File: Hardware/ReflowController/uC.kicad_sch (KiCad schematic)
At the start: 8 parts

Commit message: work on uC circuit. pin selection for the different IOs still pending
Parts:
- added NT10, NT11, NT12, NT13, NT14, NT15, NT16, NT17, NT18, NT19, NT2, NT20, NT3, NT8, NT9: NetTie_2, symbol Device:NetTie_2
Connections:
- new net FAN_1_EN: NT15.2
- new net FAN_2_EN: NT17.2
- new net HSS_1_EN: NT9.2
- new net HSS_2_EN: NT10.2
- new net HSS_3_EN: NT11.2
- new net HSS_4_EN: NT12.2
- new net PWM_BUZZER: NT2.2
- new net PWM_FAN_1: NT16.2
- new net PWM_FAN_2: NT18.2
- new net RELAY_1: NT13.2
- new net RELAY_2: NT14.2
- new net RESET_UI: NT8.2
- new net ~{INT_EMERGENCY_STOP}: NT19.2
- new net ~{INT_IO_EXPANDER}: NT3.2
- new net ~{TEMP_DATA_READY}: NT20.2
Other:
- note added: "FAN"
- note added: "IO"
- note added: "TEMP"
- note added: "UI"
- moved on the sheet: A1, NT1, NT4, NT5, NT6, NT7, R2

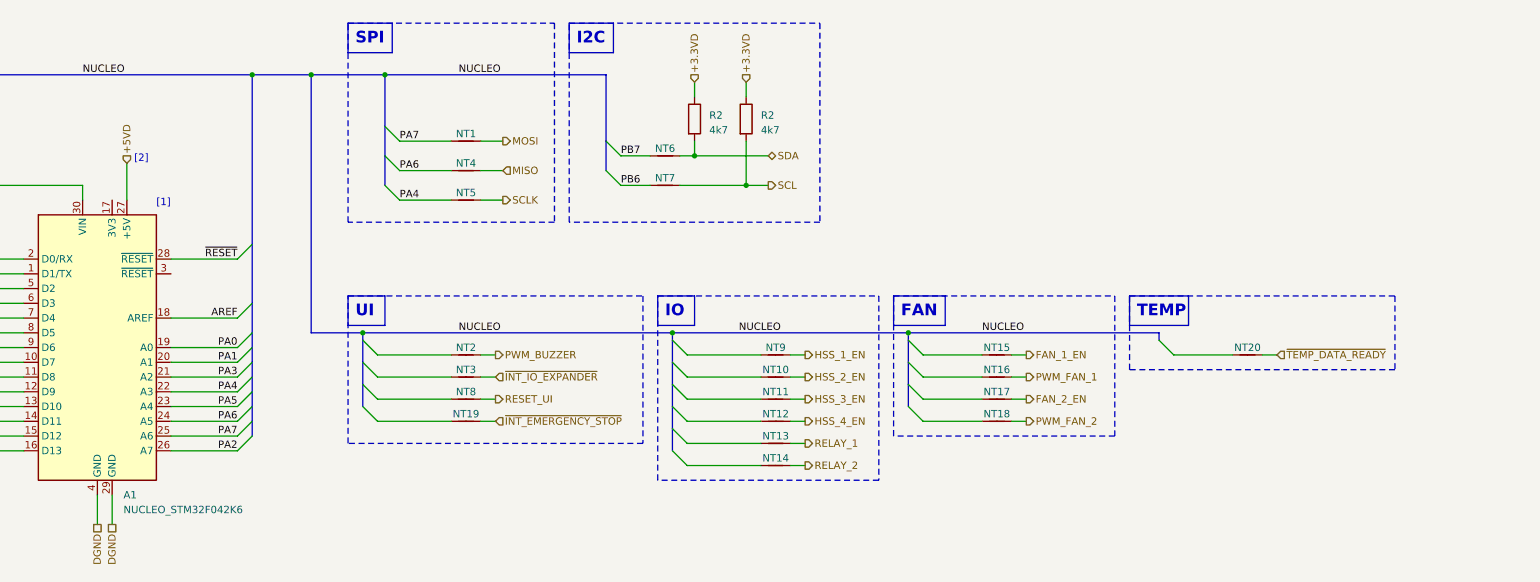
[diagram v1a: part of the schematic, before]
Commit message: work on pin assignment and porttable
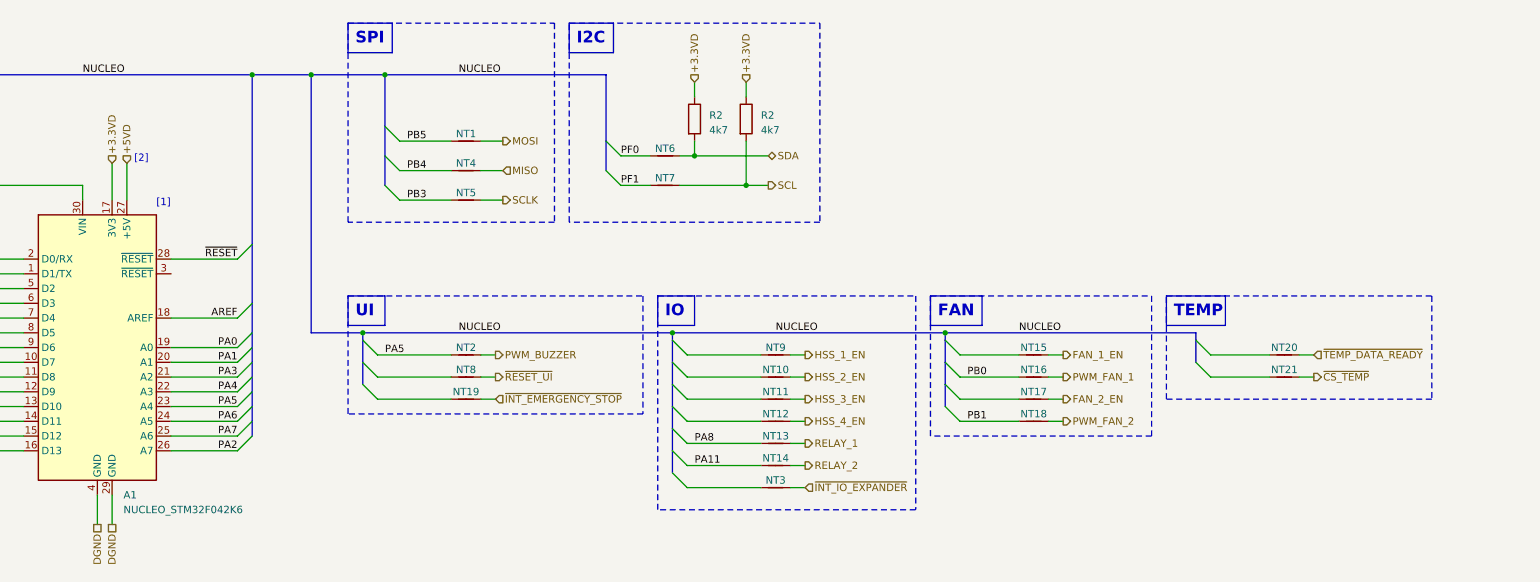
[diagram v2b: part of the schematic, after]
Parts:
- added NT21: NetTie_2, symbol Device:NetTie_2
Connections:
- net +3.3VD: now also A1.17 (3V3)
- net PA11: now also NT14.1
- net PA4: no longer NT5.1
- net PA5: now also NT2.1
- net PA6: no longer NT4.1
- net PA7: no longer NT1.1
- net PA8: now also NT13.1
- net PB0: now also NT16.1
- net PB1: now also NT18.1
- net PB3: now also NT5.1
- net PB4: now also NT4.1
- net PB5: now also NT1.1
- net PB6: no longer NT7.1
- net PB7: no longer NT6.1
- net PF0: now also NT6.1
- net PF1: now also NT7.1
- net RESET_UI renamed ~{RESET_UI}
- new net ~{CS_TEMP}: NT21.2
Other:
- moved on the sheet: NT15, NT16, NT17, NT18, NT19, NT20, NT8

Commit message: work on port table
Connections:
- net PA0: now also NT20.1
- net PA1: now also NT3.1
- net PA12: now also NT8.1
- net PA2: now also NT19.1
- net PA3: now also NT9.1
- net PA4: now also NT10.1
- net PA6: now also NT11.1, NT17.1
- net PA7: now also NT12.1, NT15.1
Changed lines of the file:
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@@
+    (effects (font (size 1.27 1.27)) (justify left bottom))
+  )
+  (label "PA4" (at 154.94 115.57 0) (fields_autoplaced)
     (effects (font (size 1.27 1.27)) (justify left bottom))
   )
@@
   )
   (label "PB3" (at 105.41 85.09 0) (fields_autoplaced)
+    (effects (font (size 1.27 1.27)) (justify left bottom))
+  )
+  (label "PA12" (at 101.6 115.57 0) (fields_autoplaced)
     (effects (font (size 1.27 1.27)) (justify left bottom))
   )
@@
     (effects (font (size 1.27 1.27)) (justify left bottom))
   )
+  (label "PA2" (at 101.6 119.38 0) (fields_autoplaced)
+    (effects (font (size 1.27 1.27)) (justify left bottom))
+  )
+  (label "PA1" (at 154.94 134.62 0) (fields_autoplaced)
+    (effects (font (size 1.27 1.27)) (justify left bottom))
+  )
   (label "NUCLEO" (at 114.3 63.5 0) (fields_autoplaced)
     (effects (font (size 1.27 1.27)) (justify left bottom))
@@
   )
   (label "NUCLEO" (at 210.82 107.95 0) (fields_autoplaced)
+    (effects (font (size 1.27 1.27)) (justify left bottom))
+  )
+  (label "PA7" (at 154.94 123.19 0) (fields_autoplaced)
     (effects (font (size 1.27 1.27)) (justify left bottom))
   )
@@
     (effects (font (size 1.27 1.27)) (justify left bottom))
   )
+  (label "PA6" (at 154.94 119.38 0) (fields_autoplaced)
+    (effects (font (size 1.27 1.27)) (justify left bottom))
+  )
   (label "PA0" (at 76.2 110.49 180) (fields_autoplaced)
     (effects (font (size 1.27 1.27)) (justify right bottom))
@@
     (effects (font (size 1.27 1.27)) (justify left bottom))
   )
+  (label "PA0" (at 245.11 111.76 0) (fields_autoplaced)
+    (effects (font (size 1.27 1.27)) (justify left bottom))
+  )
   (label "PA2" (at 76.2 128.27 180) (fields_autoplaced)
     (effects (font (size 1.27 1.27)) (justify right bottom))
   )
   (label "NUCLEO" (at 114.3 107.95 0) (fields_autoplaced)
+    (effects (font (size 1.27 1.27)) (justify left bottom))
+  )
+  (label "PA7" (at 201.93 111.76 0) (fields_autoplaced)
     (effects (font (size 1.27 1.27)) (justify left bottom))
   )
@@
     (effects (font (size 1.27 1.27)) (justify left bottom))
   )
+  (label "PA3" (at 154.94 111.76 0) (fields_autoplaced)
+    (effects (font (size 1.27 1.27)) (justify left bottom))
+  )
   (label "PA8" (at 27.94 118.11 0) (fields_autoplaced)
     (effects (font (size 1.27 1.27)) (justify left bottom))
@@
     (effects (font (size 1.27 1.27)) (justify left bottom))
   )
+  (label "PA6" (at 201.93 119.38 0) (fields_autoplaced)
+    (effects (font (size 1.27 1.27)) (justify left bottom))
+  )

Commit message: work on io adaption
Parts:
- removed NT11, NT12, NT9: NetTie_2, symbol Device:NetTie_2
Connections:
- net PA4: no longer NT10.1
- net HSS_2_EN: no longer names the net of NT10.2
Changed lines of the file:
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@@
-    (stroke (width 0) (type default))
-  )
-  (wire (pts (xy 153.67 115.57) (xy 166.37 115.57))
     (stroke (width 0) (type default))
   )
@@
     (stroke (width 0) (type default))
   )
-  (wire (pts (xy 153.67 111.76) (xy 166.37 111.76))
-    (stroke (width 0) (type default))
-  )
   (wire (pts (xy 27.94 123.19) (xy 39.37 123.19))
     (stroke (width 0) (type default))
@@
     (stroke (width 0) (type default))
   )
-  (wire (pts (xy 153.67 123.19) (xy 166.37 123.19))
-    (stroke (width 0) (type default))
-  )
   (bus (pts (xy 88.9 63.5) (xy 101.6 63.5))
     (stroke (width 0) (type default))
@@
     (stroke (width 0) (type default))
   )
-  (wire (pts (xy 171.45 123.19) (xy 173.99 123.19))
-    (stroke (width 0) (type default))
-  )
   (wire (pts (xy 27.94 95.25) (xy 39.37 95.25))
     (stroke (width 0) (type default))
@@
     (stroke (width 0) (type default))
   )
-  (wire (pts (xy 171.45 119.38) (xy 173.99 119.38))
-    (stroke (width 0) (type default))
-  )
   (wire (pts (xy 49.53 85.09) (xy 49.53 82.55))
     (stroke (width 0) (type default))
@@
     (stroke (width 0) (type default))
   )
-  (wire (pts (xy 153.67 119.38) (xy 166.37 119.38))
-    (stroke (width 0) (type default))
-  )
   (wire (pts (xy 76.2 113.03) (xy 64.77 113.03))
     (stroke (width 0) (type default))
@@
     (stroke (width 0) (type default))
   )
-  (wire (pts (xy 171.45 111.76) (xy 173.99 111.76))
-    (stroke (width 0) (type default))
-  )
   (wire (pts (xy 200.66 111.76) (xy 210.82 111.76))
     (stroke (width 0) (type default))
@@
   )
   (wire (pts (xy 54.61 78.74) (xy 54.61 85.09))
-    (stroke (width 0) (type default))
-  )
-  (wire (pts (xy 171.45 115.57) (xy 173.99 115.57))
     (stroke (width 0) (type default))
   )
@@
     (effects (font (size 1.27 1.27)) (justify left))
   )
-  (hierarchical_label "HSS_3_EN" (shape output) (at 173.99 119.38 0) (fields_autoplaced)
-    (effects (font (size 1.27 1.27)) (justify left))
-  )
   (hierarchical_label "~{CS_TEMP}" (shape output) (at 261.62 115.57 0) (fields_autoplaced)
     (effects (font (size 1.27 1.27)) (justify left))
@@
     (effects (font (size 1.27 1.27)) (justify left))
   )
-  (hierarchical_label "HSS_4_EN" (shape output) (at 173.99 123.19 0) (fields_autoplaced)
-    (effects (font (size 1.27 1.27)) (justify left))
-  )
   (hierarchical_label "FAN_1_EN" (shape output) (at 218.44 111.76 0) (fields_autoplaced)
     (effects (font (size 1.27 1.27)) (justify left))
@@
   )
   (hierarchical_label "RELAY_2" (shape output) (at 173.99 130.81 0) (fields_autoplaced)
-    (effects (font (size 1.27 1.27)) (justify left))
-  )
-  (hierarchical_label "HSS_2_EN" (shape output) (at 173.99 115.57 0) (fields_autoplaced)
-    (effects (font (size 1.27 1.27)) (justify left))
-  )
-  (hierarchical_label "HSS_1_EN" (shape output) (at 173.99 111.76 0) (fields_autoplaced)
     (effects (font (size 1.27 1.27)) (justify left))
   )
@@
     )
   )
-  (symbol (lib_id "Device:NetTie_2") (at 168.91 111.76 0) (unit 1)
-    (in_bom yes) (on_board yes) (dnp no)
-    (property "Reference" "NT9" (at 168.91 110.49 0)
-      (effects (font (size 1.27 1.27)))
-    )
-    (property "Value" "NetTie_2" (at 168.91 113.03 0)
-      (effects (font (size 1.27 1.27)) hide)
-    )
-    (property "Footprint" "" (at 168.91 111.76 0)
-      (effects (font (size 1.27 1.27)) hide)
-    )
-    (property "Datasheet" "~" (at 168.91 111.76 0)
-      (effects (font (size 1.27 1.27)) hide)
-    )
-    (pin "1")
-    (pin "2")
-    (instances
-      (project "ReflowController"
-        (path "/2394cc2a-b9b0-4c0b-be11-1fc6085b0d5c/7f3c5223-ce8d-4c24-a6f4-4e6402f9b436"
-          (reference "NT9") (unit 1)
-        )
-      )
-    )
-  )
-  (symbol (lib_id "Device:NetTie_2") (at 168.91 123.19 0) (unit 1)
-    (in_bom yes) (on_board yes) (dnp no)
-    (property "Reference" "NT12" (at 168.91 121.92 0)
-      (effects (font (size 1.27 1.27)))
-    )
-    (property "Value" "NetTie_2" (at 168.91 124.46 0)
-      (effects (font (size 1.27 1.27)) hide)
-    )
-    (property "Footprint" "" (at 168.91 123.19 0)
-      (effects (font (size 1.27 1.27)) hide)
-    )
-    (property "Datasheet" "~" (at 168.91 123.19 0)
-      (effects (font (size 1.27 1.27)) hide)
-    )
-    (pin "1")
-    (pin "2")
-    (instances
-      (project "ReflowController"
-        (path "/2394cc2a-b9b0-4c0b-be11-1fc6085b0d5c/7f3c5223-ce8d-4c24-a6f4-4e6402f9b436"
-          (reference "NT12") (unit 1)
-        )
-      )
-    )
-  )
   (symbol (lib_id "Device:NetTie_2") (at 115.57 119.38 0) (unit 1)
     (in_bom yes) (on_board yes) (dnp no)
@@
         )
       )
-    )
-  )
-  (symbol (lib_id "Device:NetTie_2") (at 168.91 119.38 0) (unit 1)
-    (in_bom yes) (on_board yes) (dnp no)
-    (property "Reference" "NT11" (at 168.91 118.11 0)
-      (effects (font (size 1.27 1.27)))
-    )
-    (property "Value" "NetTie_2" (at 168.91 120.65 0)
-      (effects (font (size 1.27 1.27)) hide)
-    )
-    (property "Footprint" "" (at 168.91 119.38 0)
-      (effects (font (size 1.27 1.27)) hide)
-    )
-    (property "Datasheet" "~" (at 168.91 119.38 0)
-      (effects (font (size 1.27 1.27)) hide)
-    )
-    (pin "1")
-    (pin "2")
-    (instances
-      (project "ReflowController"
-        (path "/2394cc2a-b9b0-4c0b-be11-1fc6085b0d5c/7f3c5223-ce8d-4c24-a6f4-4e6402f9b436"
-          (reference "NT11") (unit 1)
-        )
-      )

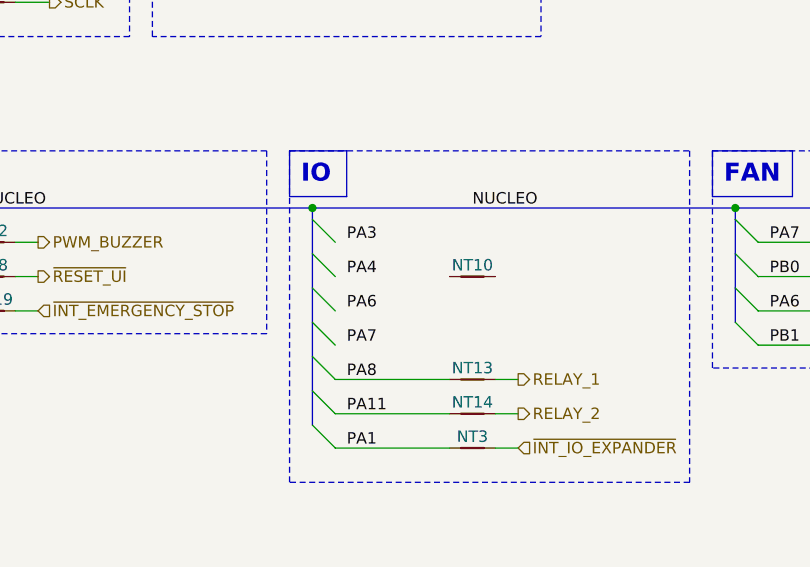
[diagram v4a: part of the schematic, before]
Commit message: changed port table + updated schema
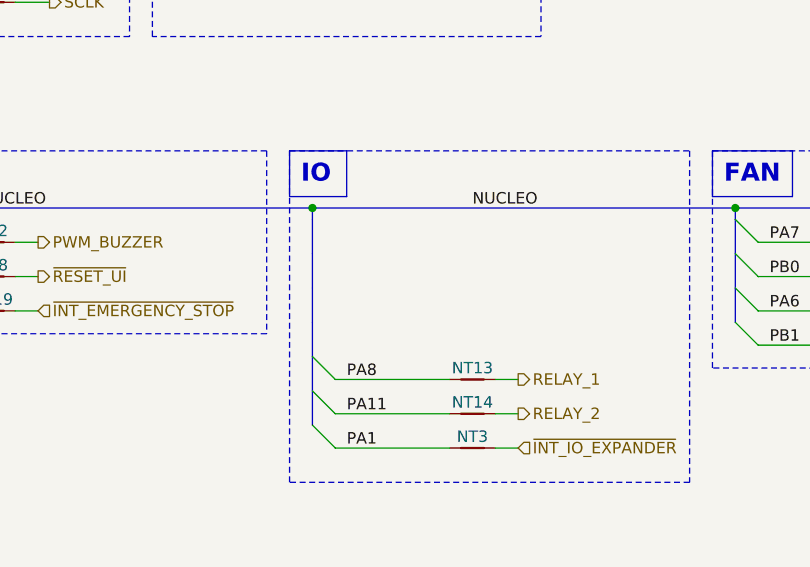
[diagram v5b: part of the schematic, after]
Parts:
- removed NT10: NetTie_2, symbol Device:NetTie_2
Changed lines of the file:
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@@
   (junction (at 97.79 107.95) (diameter 0) (color 0 0 0 0)
   )
-  (bus_entry (at 151.13 113.03) (size 2.54 2.54)
-    (stroke (width 0) (type default))
-  )
   (bus_entry (at 25.4 118.11) (size 2.54 2.54)
     (stroke (width 0) (type default))
@@
     (stroke (width 0) (type default))
   )
-  (bus_entry (at 151.13 109.22) (size 2.54 2.54)
-    (stroke (width 0) (type default))
-  )
   (bus_entry (at 25.4 115.57) (size 2.54 2.54)
     (stroke (width 0) (type default))
@@
     (stroke (width 0) (type default))
   )
-  (bus_entry (at 151.13 116.84) (size 2.54 2.54)
-    (stroke (width 0) (type default))
-  )
   (bus_entry (at 25.4 102.87) (size 2.54 2.54)
     (stroke (width 0) (type default))
@@
   )
   (bus_entry (at 101.6 72.39) (size 2.54 2.54)
-    (stroke (width 0) (type default))
-  )
-  (bus_entry (at 151.13 120.65) (size 2.54 2.54)
     (stroke (width 0) (type default))
   )
@@
     (effects (font (size 1.27 1.27)) (justify left bottom))
   )
-  (label "PA4" (at 154.94 115.57 0) (fields_autoplaced)
-    (effects (font (size 1.27 1.27)) (justify left bottom))
-  )
   (label "PA11" (at 27.94 120.65 0) (fields_autoplaced)
     (effects (font (size 1.27 1.27)) (justify left bottom))
@@
     (effects (font (size 1.27 1.27)) (justify left bottom))
   )
-  (label "PA7" (at 154.94 123.19 0) (fields_autoplaced)
-    (effects (font (size 1.27 1.27)) (justify left bottom))
-  )
   (label "PA5" (at 101.6 111.76 0) (fields_autoplaced)
     (effects (font (size 1.27 1.27)) (justify left bottom))
@@
     (effects (font (size 1.27 1.27)) (justify left bottom))
   )
-  (label "PA6" (at 154.94 119.38 0) (fields_autoplaced)
-    (effects (font (size 1.27 1.27)) (justify left bottom))
-  )
   (label "PA0" (at 76.2 110.49 180) (fields_autoplaced)
     (effects (font (size 1.27 1.27)) (justify right bottom))
@@
   )
   (label "PB0" (at 201.93 115.57 0) (fields_autoplaced)
-    (effects (font (size 1.27 1.27)) (justify left bottom))
-  )
-  (label "PA3" (at 154.94 111.76 0) (fields_autoplaced)
     (effects (font (size 1.27 1.27)) (justify left bottom))
   )
@@
         )
       )
-    )
-  )
-  (symbol (lib_id "Device:NetTie_2") (at 168.91 115.57 0) (unit 1)
-    (in_bom yes) (on_board yes) (dnp no)
-    (property "Reference" "NT10" (at 168.91 114.3 0)
-      (effects (font (size 1.27 1.27)))
-    )
-    (property "Value" "NetTie_2" (at 168.91 116.84 0)
-      (effects (font (size 1.27 1.27)) hide)
-    )
-    (property "Footprint" "" (at 168.91 115.57 0)
-      (effects (font (size 1.27 1.27)) hide)
-    )
-    (property "Datasheet" "~" (at 168.91 115.57 0)
-      (effects (font (size 1.27 1.27)) hide)
-    )
-    (pin "1")
-    (pin "2")
-    (instances
-      (project "ReflowController"
-        (path "/2394cc2a-b9b0-4c0b-be11-1fc6085b0d5c/7f3c5223-ce8d-4c24-a6f4-4e6402f9b436"
-          (reference "NT10") (unit 1)
-        )
-      )
